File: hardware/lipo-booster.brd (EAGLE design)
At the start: 21.6 x 36.8 mm, 33 parts, among them IC1 MCP73833-UN, J2 USB, Q1 BSS84, Q2 BSS84, U1 TEXAS_INSTRUMENTS_TPS61032PWP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

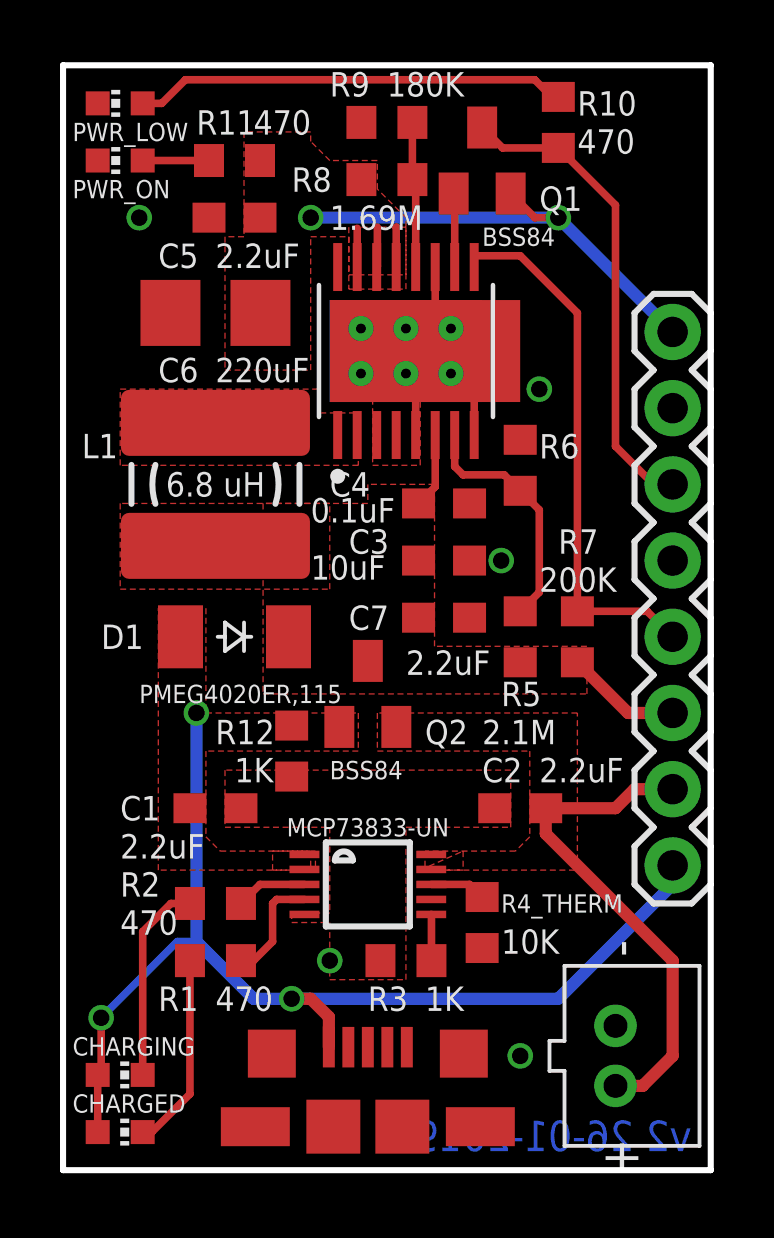
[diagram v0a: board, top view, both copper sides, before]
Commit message: Updated design with pcb layout suggestions from reddit thread
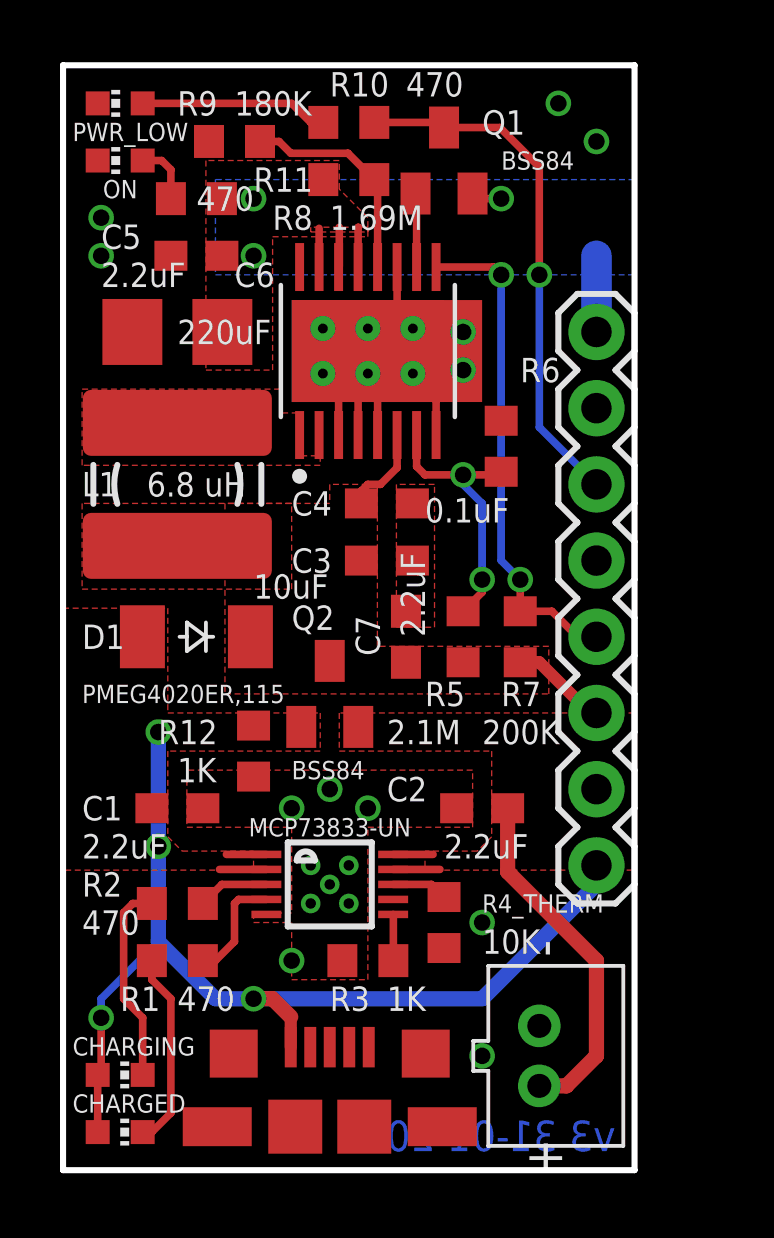
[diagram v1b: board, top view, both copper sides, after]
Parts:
- LED4: value PWR_ON -> ON
- moved R10 6.99 mm to (9.53, 34.9), turned to 0 degrees
- moved R9 5.12 mm to (5.71, 34.3)
- moved J1 2.54 mm to (17.8, 10.2)
- moved J3 2.54 mm to (15.9, 3.81)
- moved C3 1.90 mm to (10.8, 20.3)
- moved C4 1.90 mm to (10.8, 22.2)
- moved R5 1.90 mm to (13.3, 17.8)
- moved R7 1.90 mm to (15.2, 17.8)
- moved R11 1.80 mm to (4.45, 32.4)
- moved C5 1.80 mm to (4.45, 30.5)
- moved C6 1.42 mm to (3.81, 27.9)
- moved C7 1.42 mm to (11.4, 17.8), turned to 90 degrees
- moved Q1 1.27 mm to (12.7, 33.7)
- moved R4_THERM 1.27 mm to (12.7, 8.26)
- moved R12 1.27 mm to (6.35, 14.0)
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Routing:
- net +5V: track 19.5 -> 7.52 mm, vias 2 -> 3
- net N$3: track 14.4 -> 6.28 mm
- net N$33: track 4.87 -> 7.30 mm
- net VBAT: track 16.8 -> 14.7 mm
- net PWR_LBO: track 16.0 -> 17.5 mm, vias 0 -> 1
- net PWR_EN: track 18.1 -> 16.6 mm, vias 0 -> 2
- net N$30: track 8.11 -> 9.10 mm, vias 0 -> 2
- net GND: track 17.1 -> 17.6 mm, vias 5 -> 17
- net VBUS: track 37.1 -> 37.2 mm, vias 3 -> 4
- added copper zone on layer 16, net +5V
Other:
- board size 21.6 x 36.8 mm -> 19.1 x 36.8 mm
- board text added: "v3 31-01-2019"
- board text removed: "v2 26-01-2019"

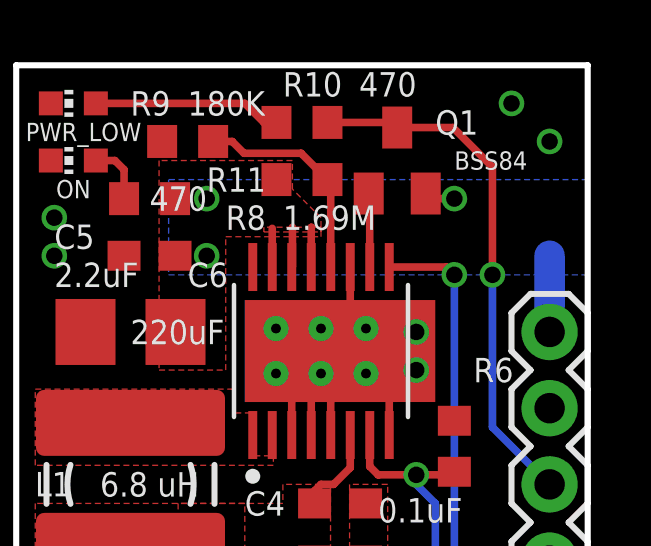
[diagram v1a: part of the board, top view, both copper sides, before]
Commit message: Small change to schematic to change transistor and update of photo
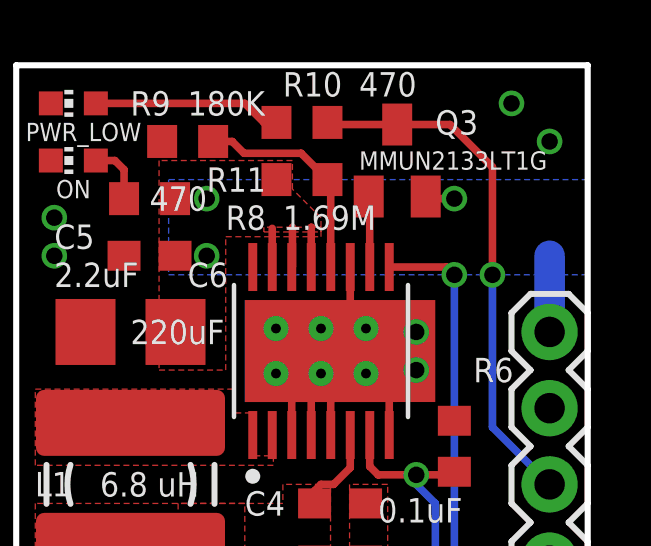
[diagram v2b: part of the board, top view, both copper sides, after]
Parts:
- removed Q1: BSS84, transistor-small-signal:SOT23
- added Q3: MMUN2133LT1G, transistor-pnp:SC59-BEC
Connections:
- net +5V: now also Q3.E; no longer Q1.2
- net N$32: now also Q3.B; no longer Q1.1
- net PWR_LBO: now also Q3.C; no longer Q1.3
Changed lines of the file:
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@@
 <attribute name="VALUE" x="7.62" y="13.335" size="0.6096" layer="25" align="center-left"/>
-</element>
-<element name="Q1" library="transistor-small-signal" library_urn="urn:adsk.eagle:library:401" package="SOT23" package3d_urn="urn:adsk.eagle:package:28738/2" value="BSS84" x="12.7" y="33.655" smashed="yes">
-<attribute name="NAME" x="13.97" y="34.925" size="0.8128" layer="25" align="center-left"/>
-<attribute name="VALUE" x="14.605" y="33.655" size="0.6096" layer="25" align="center-left"/>
 </element>
 <element name="J2" library="audio amplifier example" library_urn="urn:adsk.eagle:library:970892" package="1981584-1" package3d_urn="urn:adsk.eagle:package:970926/2" value="USB" x="8.89" y="0" smashed="yes">
@@
 </element>
 <element name="J3" library="adafruit" library_urn="urn:adsk.eagle:library:420" package="JST-PH-2-THM" package3d_urn="urn:adsk.eagle:package:6240693/1" value="" x="15.875" y="3.81" smashed="yes" rot="R270"/>
+<element name="Q3" library="transistor-pnp" library_urn="urn:adsk.eagle:library:399" package="SC59-BEC" package3d_urn="urn:adsk.eagle:package:28754/2" value="MMUN2133LT1G" x="12.7" y="33.655" smashed="yes">
+<attribute name="NAME" x="13.97" y="34.925" size="0.8128" layer="25" align="center-left"/>
+<attribute name="VALUE" x="11.43" y="33.655" size="0.6096" layer="25" align="center-left"/>
+</element>
 </elements>
 <signals>
@@
 <via x="1.27" y="31.75" extent="1-16" drill="0.55"/>
 <wire x1="12.435" y1="25.665" x2="12.435" y2="24.505" width="0.254" layer="1"/>
-<wire x1="10.795" y1="27.305" x2="10.795" y2="26.97500625" width="0.254" layer="1"/>
 <via x="7.62" y="6.985" extent="1-16" drill="0.55"/>
 <via x="13.335" y="27.94" extent="1-16" drill="0.55"/>
@@
 <wire x1="9.835" y1="31.425" x2="9.8425" y2="31.4325" width="0.254" layer="1"/>
 <contactref element="J1" pad="8"/>
-<contactref element="Q1" pad="2"/>
 <polygon width="0.254" layer="1">
 <vertex x="6.985" y="31.115"/>
@@
 </polygon>
 <via x="14.605" y="32.385" extent="1-16" drill="0.55"/>
-<wire x1="13.65" y1="32.555" x2="13.82" y2="32.385" width="0.254" layer="1"/>
-<wire x1="13.82" y1="32.385" x2="14.605" y2="32.385" width="0.254" layer="1"/>
 <wire x1="17.78" y1="27.94" x2="17.78" y2="30.48" width="1.016" layer="16"/>
 <polygon width="0.254" layer="16">
@@
 <via x="6.35" y="32.385" extent="1-16" drill="0.55"/>
 <via x="6.35" y="30.48" extent="1-16" drill="0.55"/>
+<contactref element="Q3" pad="E"/>
+<wire x1="14.605" y1="32.385" x2="13.72" y2="32.385" width="0.254" layer="1"/>
+<wire x1="13.72" y1="32.385" x2="13.65" y2="32.455" width="0.254" layer="1"/>
 </signal>
 <signal name="N$17">
@@
 <contactref element="J1" pad="6"/>
 <contactref element="R10" pad="2"/>
-<contactref element="Q1" pad="3"/>
-<wire x1="15.875" y1="33.44" x2="14.56" y2="34.755" width="0.254" layer="1"/>
-<wire x1="12.7" y1="34.755" x2="12.53" y2="34.925" width="0.254" layer="1"/>
-<wire x1="12.53" y1="34.925" x2="10.375" y2="34.925" width="0.254" layer="1"/>
-<wire x1="12.7" y1="34.755" x2="14.56" y2="34.755" width="0.254" layer="1"/>
 <wire x1="17.78" y1="22.86" x2="15.875" y2="24.765" width="0.254" layer="16"/>
 <wire x1="15.875" y1="24.765" x2="15.875" y2="29.845" width="0.254" layer="16"/>
 <via x="15.875" y="29.845" extent="1-16" drill="0.55"/>
 <wire x1="15.875" y1="33.44" x2="15.875" y2="29.845" width="0.254" layer="1"/>
+<contactref element="Q3" pad="C"/>
+<wire x1="12.7" y1="34.855" x2="14.46" y2="34.855" width="0.254" layer="1"/>
+<wire x1="14.46" y1="34.855" x2="15.875" y2="33.44" width="0.254" layer="1"/>
+<wire x1="12.7" y1="34.855" x2="10.445" y2="34.855" width="0.254" layer="1"/>
+<wire x1="10.445" y1="34.855" x2="10.375" y2="34.925" width="0.254" layer="1"/>
 </signal>
 <signal name="PWR_EN">
@@
 <signal name="N$32">
 <contactref element="U1" pad="10"/>
-<contactref element="Q1" pad="1"/>
-<wire x1="11.785" y1="30.105" x2="11.785" y2="32.52" width="0.254" layer="1"/>
-<wire x1="11.785" y1="32.52" x2="11.75" y2="32.555" width="0.254" layer="1"/>
+<contactref element="Q3" pad="B"/>
+<wire x1="11.785" y1="30.105" x2="11.785" y2="32.42" width="0.254" layer="1"/>
+<wire x1="11.785" y1="32.42" x2="11.75" y2="32.455" width="0.254" layer="1"/>
 </signal>
 <signal name="N$33">
